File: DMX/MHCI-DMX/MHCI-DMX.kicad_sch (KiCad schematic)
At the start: 39 parts, among them J1 XLR_Male, J2 XLR5_Female, J3 2012670005, J4 Barrel_Jack, K2 G5V-2, U2 TJA1051T, U4 74LVC1G08

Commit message: DMX Schematic complete, and initial Layout
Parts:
- removed C7: 10uF, Capacitor_SMD:C_0603_1608Metric, symbol Device:C_Small
- removed C8: 1uF, Capacitor_SMD:C_0402_1005Metric, symbol Device:C_Small
- removed C9: 100nF, Capacitor_SMD:C_0402_1005Metric, symbol Device:C_Small
- removed D1: D_TVS_Dual_AAC, Package_TO_SOT_SMD:SOT-23, symbol Device:D_TVS_Dual_AAC
- removed FB2: FerriteBead, Diode_SMD:D_0805_2012Metric, symbol Device:FerriteBead_Small
- removed J4: Barrel_Jack, Connector_BarrelJack:BarrelJack_SwitchcraftConxall_RAPC10U_Horizontal, symbol Connector:Barrel_Jack
- removed TP3: VIN, TestPoint:TestPoint_Pad_D1.0mm, symbol Connector:TestPoint
- removed TP4: 5V, TestPoint:TestPoint_Pad_D1.0mm, symbol Connector:TestPoint
- removed U1: ~, MHCI:ESP-32-S3-Zero - SMD, symbol MHCI:ESP32-S3-Zero
- added D1: 1N4148W, Diode_SMD:D_SOD-123, symbol Device:D
- added D2, D4, D6: D_TVS_Dual_AAC, Package_TO_SOT_SMD:SOT-23, symbol Device:D_TVS_Dual_AAC
- added J10, J11, J12, J13, J14, J15: Conn_01x02, MHCI:2060-452-998-404 Wago, symbol Connector_Generic:Conn_01x02
- added J17: Conn_01x08, Connector_PinSocket_2.54mm:PinSocket_1x08_P2.54mm_Vertical, symbol Connector_Generic:Conn_01x08
- added J4, J7, J8: Conn_01x04, Connector_PinSocket_2.54mm:PinSocket_1x04_P2.54mm_Vertical, symbol Connector_Generic:Conn_01x04
- added J5: Conn_01x02, TerminalBlock_Phoenix:TerminalBlock_Phoenix_MPT-0,5-2-2.54_1x02_P2.54mm_Horizontal, symbol Connector_Generic:Conn_01x02
- added J6: Barrel_Jack_MountingPin, Connector_BarrelJack:BarrelJack_GCT_DCJ200-10-A_Horizontal, symbol Connector:Barrel_Jack_MountingPin
- added J9: Conn_01x02, Connector_PinHeader_2.54mm:PinHeader_1x02_P2.54mm_Vertical, symbol Connector_Generic:Conn_01x02
- added JP10, JP11, JP12, JP9: SolderJumper_3_Open, Jumper:SolderJumper-3_P1.3mm_Open_RoundedPad1.0x1.5mm, symbol Jumper:SolderJumper_3_Open
- added JP7, JP8: Jumper_2_Open, Jumper:SolderJumper-2_P1.3mm_Open_RoundedPad1.0x1.5mm, symbol Jumper:Jumper_2_Open
- added Q1: PMOS, Package_TO_SOT_SMD:SOT-23, symbol Simulation_SPICE:PMOS
- added R8: 100k, Resistor_SMD:R_0603_1608Metric, symbol Device:R_US
- added R9: 120R, Resistor_SMD:R_0402_1005Metric, symbol Device:R_US
- added U1, U6, U9: SRV05-4, Package_TO_SOT_SMD:SOT-23-6, symbol Power_Protection:SRV05-4
- added U5: TME-0505S, Converter_DCDC:Converter_DCDC_TRACO_TME_03xxS_05xxS_12xxS_Single_THT, symbol Converter_DCDC:TME-0305S
- added U7: ~, MHCI:ESP-32-S3-Tiny - PTH, symbol MHCI:ESP32-S3-Tiny
- added U8: TXB0108PW, Package_SO:TSSOP-20_4.4x6.5mm_P0.65mm, symbol Logic_LevelTranslator:TXB0108PW
- J1: footprint Connector_Audio:Jack_XLR_Neutrik_NC5FAH-DA_Horizontal -> MHCI:Jack_XLR_Neutrik_NC5MAH_LR
- J2: footprint Connector_Audio:Jack_XLR_Neutrik_NC5FAH-0_Horizontal -> MHCI:Jack_XLR_Neutrik_NC5FAH_LR-DAE
- J3: footprint Landing-Light:MOLEX_2012670005 -> LandingLight:MOLEX_2012670005
- PS1: footprint MCHI:CONV_TBA1-0510 -> MHCI:CONV_TBA1-0510
- U3: footprint (none) -> MHCI:ISO-DMX
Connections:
- net +3V3: now also U7.3V3
- net +5V: now also K2.16, D1.1 (K), J17.1 (Pin_1), J4.1 (Pin_1), J7.1 (Pin_1), J8.1 (Pin_1), U1.5 (VP), U5.2 (+Vin), U6.5 (VP), U9.5 (VP)
- net A: now also R9.1
- net A_OUT: now also D4.1 (A1)
- net B: now also JP8.2 (B)
- net B_OUT: now also D4.2 (A2)
- net CANH: now also JP11.3 (B), JP9.3 (B), U6.6 (IO4)
- net CANL: now also JP10.1 (A), JP12.1 (A), U6.4 (IO3)
- net CAN_RX: now also U7.2 (GPIO2)
- net CAN_S: now also U7.5 (GPIO5)
- net CAN_TX: now also U7.1 (GPIO1)
- net CC1: now also D2.2 (A2)
- net CC2: now also D2.1 (A1)
- net D: now also U7.14 (GPIO14)
- net DE: now also U7.15 (GPIO15)
- net ESP_32_GPIO_12: now also U7.12 (GPIO12)
- net ESP_32_GPIO_13: now also U7.13 (GPIO13)
- net Earth: now also D2.3 (common), J5.2 (Pin_2), J6.2, J9.2 (Pin_2)
- net GND: now also U3.2 (GND), D6.3 (common), J10.2 (Pin_2), J11.2 (Pin_2), J12.2 (Pin_2), J13.2 (Pin_2), J14.2 (Pin_2), J15.2 (Pin_2), J17.8 (Pin_8), J4.4 (Pin_4), J7.4 (Pin_4), J8.4 (Pin_4), JP7.2 (B), Q1.2 (S), R8.2, U1.2 (VN), U5.1 (-Vin), U6.2 (VN), U7.GND, U9.2 (VN)
- net GND_DMX: now also D4.3 (common), U5.3 (-Vout)
- net NRE: now also U7.16 (GPIO16)
- net R: now also U7.17 (GPIO17)
- net SCL: now also U7.3 (GPIO3), U8.1 (A1)
- net SDA: now also U7.4 (GPIO4), U8.3 (A2)
- net VIN: now also J5.1 (Pin_1), J6.1, J9.1 (Pin_1)
- net DMX_EN: now reaches U4.2
- net DMX_EN: now also U7.18 (GPIO18)
- net at U4.4: now also Q1.1 (G), R8.1; no longer K2.16
- net at JP1.1 (A): now also U7.5V
- net +5V_ISO: now reaches U3.7 (5V_ISO)
- net +5V_ISO: now also U5.4 (+Vout)
- net DMX_PASSTHROUGH: now reaches K2.1
- net DMX_PASSTHROUGH: now also D1.2 (A), JP7.1 (A), Q1.3 (D)
- new net: J7.3 (Pin_3), JP12.2 (C)
- new net: J7.2 (Pin_2), JP11.2 (C)
- new net: JP8.1 (A), R9.2
- new net: J4.2 (Pin_2), JP9.2 (C)
- new net: J4.3 (Pin_3), JP10.2 (C)
- new net GPIO_X1: U7.6 (GPIO6), U8.4 (A3)
- new net GPIO_X1_5: J10.1 (Pin_1), J17.2 (Pin_2), U1.1 (IO1), U8.17 (B3)
- new net GPIO_X2: U7.7 (GPIO7), U8.5 (A4)
- new net GPIO_X2_5: J11.1 (Pin_1), J17.3 (Pin_3), U1.3 (IO2), U8.16 (B4)
- new net GPIO_X3: U7.8 (GPIO8), U8.6 (A5)
- new net GPIO_X3_5: J12.1 (Pin_1), J17.4 (Pin_4), U1.4 (IO3), U8.15 (B5)
- new net GPIO_X4: U7.9 (GPIO9), U8.7 (A6)
- new net GPIO_X4_5: J13.1 (Pin_1), J17.5 (Pin_5), U1.6 (IO4), U8.14 (B6)
- new net GPIO_X5: U7.11 (GPIO11), U8.8 (A7)
- new net GPIO_X5_5: J14.1 (Pin_1), J17.6 (Pin_6), U8.13 (B7), U9.1 (IO1)
- new net GPIO_X6: U7.10 (GPIO10), U8.9 (A8)
- new net GPIO_X6_5: J15.1 (Pin_1), J17.7 (Pin_7), U8.12 (B8), U9.3 (IO2)
- new net SCL_5: JP11.1 (A), JP9.1 (A), U6.1 (IO1), U8.20 (B1)
- new net SDA_5: JP10.3 (B), JP12.3 (B), U6.3 (IO2), U8.18 (B2)
- new net UART_RX: J8.3 (Pin_3), U7.RX, U9.4 (IO3)
- new net UART_TX: J8.2 (Pin_2), U7.TX, U9.6 (IO4)
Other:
- note added: "Connectors"
- note added: "Expose full GPIO"
- note added: "Mosfet and driver pins for LED tape"
- note added: "Some 1 Pin Data ports"
- note removed: "Connector"
- note removed: "OR Gate"
- note removed: "Termination Resistor"
- moved on the sheet: C1, C2, C3, C4, C5, C6, FB1, J1, J2, J3, JP1, JP2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

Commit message: MHCI DMX - Finalise schematic and initial layout routing
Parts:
- removed JP10, JP11, JP12, JP9: SolderJumper_3_Open, Jumper:SolderJumper-3_P1.3mm_Open_RoundedPad1.0x1.5mm, symbol Jumper:SolderJumper_3_Open
- removed K2: G5V-2, Relay_THT:Relay_DPDT_Omron_G5V-2, symbol Relay:G5V-2
- removed PS1: TBA1-0510, MHCI:CONV_TBA1-0510, symbol MHCI:TBA1-0510
- removed U2: TJA1051T, Package_SO:SOIC-8_3.9x4.9mm_P1.27mm, symbol Interface_CAN_LIN:TJA1051T
- removed U4: 74LVC1G08, Package_TO_SOT_SMD:SOT-23-5_HandSoldering, symbol 74xGxx:74LVC1G08
- removed U6: SRV05-4, Package_TO_SOT_SMD:SOT-23-6, symbol Power_Protection:SRV05-4
- added D3, D5: D_TVS_Dual_AAC, Package_TO_SOT_SMD:SOT-23, symbol Device:D_TVS_Dual_AAC
- added J16, J18: Conn_01x04, Connector_PinSocket_2.54mm:PinSocket_1x04_P2.54mm_Vertical, symbol Connector_Generic:Conn_01x04
- added JP13, JP14, JP15: SolderJumper_3_Open, Jumper:SolderJumper-3_P1.3mm_Open_RoundedPad1.0x1.5mm, symbol Jumper:SolderJumper_3_Open
- added K1: G6K-2, Relay_SMD:Relay_DPDT_Omron_G6K-2F, symbol Relay:G6K-2
- added U10: ~, MHCI:WirelessDMX-Module, symbol MHCI:WirelessDMX-Module
- added U11: TJA1051T-3, Package_SO:SOIC-8_3.9x4.9mm_P1.27mm, symbol Interface_CAN_LIN:TJA1051T-3
- added U4: TEC2-1210WI, Converter_DCDC:Converter_DCDC_TRACO_TMR-xxxx_THT, symbol Converter_DCDC:TEC2-1210WI
- D2, J3, R6, R7: now not fitted; now left out of the parts list
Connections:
- net +3V3: now also U3.1 (5V), U8.10 (OE), U8.2 (V_{CCA}), JP15.1 (A), U10.1 (VCC), U10.11 (VCC), U11.5 (VIO), U4.6 (+VOUT)
- net +5V: now also J16.1 (Pin_1), J18.1 (Pin_1), JP13.3 (B), JP14.3 (B), JP15.3 (B), K1.8, U11.3 (VCC), U4.2 (+VIN); no longer U3.1 (5V)
- net A: now also JP5.1 (A), K1.4; no longer JP5.2 (C)
- net A_IN: now also K1.2
- net A_OUT: now also JP5.2 (C), K1.3; no longer JP5.1 (A)
- net B: now also JP6.1 (A), K1.5; no longer JP6.2 (C)
- net B_IN: now also K1.7
- net B_OUT: now also JP6.2 (C), K1.6; no longer JP6.1 (A)
- net CANH: now also D5.1 (A1), J16.2 (Pin_2), J18.2 (Pin_2)
- net CANH_L: now also U11.6 (CANL)
- net CANH_T: now also U11.7 (CANH)
- net CANL: now also D5.2 (A2), J16.3 (Pin_3), J18.3 (Pin_3)
- net CAN_RX: now also U11.4 (RXD)
- net CAN_S: now also U11.8 (S)
- net CAN_TX: now also U11.1 (TXD)
- net D: now also U10.3 (DMX_TX)
- net DE: now also U10.4 (DMX_DE)
- net DMX_EN: now also JP13.1 (A)
- net DMX_PASSTHROUGH: now also K1.1
- net Earth: now also JP14.1 (A), U4.1 (-VIN)
- net GND: now also U8.11 (GND), D3.3 (common), D5.3 (common), J16.4 (Pin_4), J18.4 (Pin_4), U10.10 (GND), U10.12 (GND), U10.2 (GND), U11.2 (GND), U4.7 (-VOUT)
- net GPIO_X1: now also U7.11 (GPIO11), U10.9 (SPI_SCK); no longer U7.6 (GPIO6)
- net GPIO_X1_5: now also U1.3 (IO2); no longer U1.1 (IO1)
- net GPIO_X2: now also U7.10 (GPIO10), U10.8 (SPI_MOSI); no longer U7.7 (GPIO7)
- net GPIO_X2_5: now also U1.1 (IO1); no longer U1.3 (IO2)
- net GPIO_X3: now also U7.9 (GPIO9), U10.7 (SPI_MISO); no longer U7.8 (GPIO8)
- net GPIO_X4_5: now also U9.3 (IO2); no longer U1.6 (IO4)
- net GPIO_X5: now also U7.7 (GPIO7), U10.14 (SPI_nSS); no longer U7.11 (GPIO11)
- net GPIO_X5_5: now also U9.6 (IO4); no longer U9.1 (IO1)
- net GPIO_X6: now also U7.6 (GPIO6); no longer U7.10 (GPIO10)
- net GPIO_X6_5: now also U9.4 (IO3); no longer U9.3 (IO2)
- net NRE: now also U10.5 (DMX_RE)
- net R: now also U10.6 (DMX_RX)
- net SCL: now also U10.18 (I2C_SCL)
- net SCL_5: now also J4.2 (Pin_2), J7.2 (Pin_2), D3.2 (A2)
- net SDA: now also U10.17 (I2C_SDA)
- net SDA_5: now also J4.3 (Pin_3), J7.3 (Pin_3), D3.1 (A1)
- net UART_RX: now also D6.1 (A1); no longer U9.4 (IO3)
- net UART_TX: now also D6.2 (A2); no longer U9.6 (IO4)
- net at U8.19 (V_{CCB}): now also JP15.2 (C)
- net at Q1.1 (G), R8.1: now also JP13.2 (C)
- net ESP_32_GPIO_12 renamed I2C_nATTN
- net I2C_nATTN: now also U10.16 (I2C_nATTN)
- net ESP_32_GPIO_13 renamed SPI_nATTN
- net SPI_nATTN: now also U10.13 (SPI_nATTN)
- net GPIO_X4 renamed CTI_RESET
- net CTI_RESET: now also U7.8 (GPIO8), U10.15 (CTI_RESET); no longer U7.9 (GPIO9)
- new net: JP14.2 (C), U4.3 (ON/~{OFF})
- no-connect marks 19 -> 21
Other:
- note added: "Check the voltages here"
- note added: "RS3K-053.3S/H3"
- note removed: "Expose full GPIO"
- note removed: "Mosfet and driver pins for LED tape"
- note removed: "Some 1 Pin Data ports"
- moved on the sheet: C1, C2, C3, C4, C5, C6, D1, D4, D6, FB1, J1, J10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

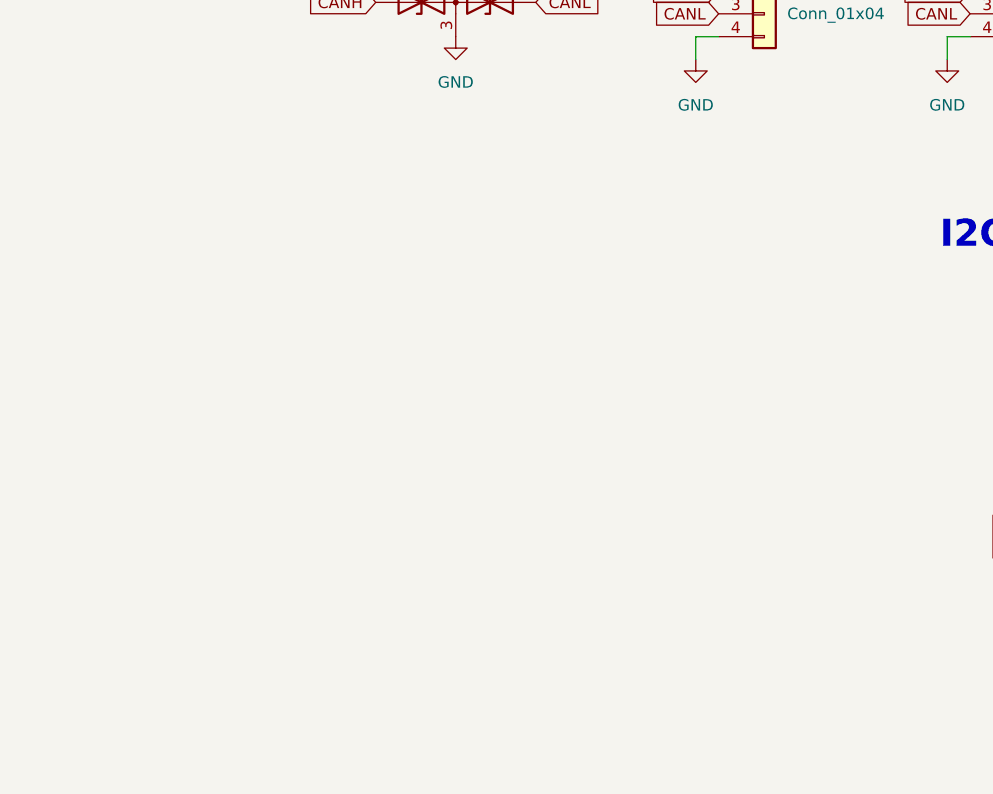
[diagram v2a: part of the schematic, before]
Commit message: Adding LEDs to DMX plug and socket.
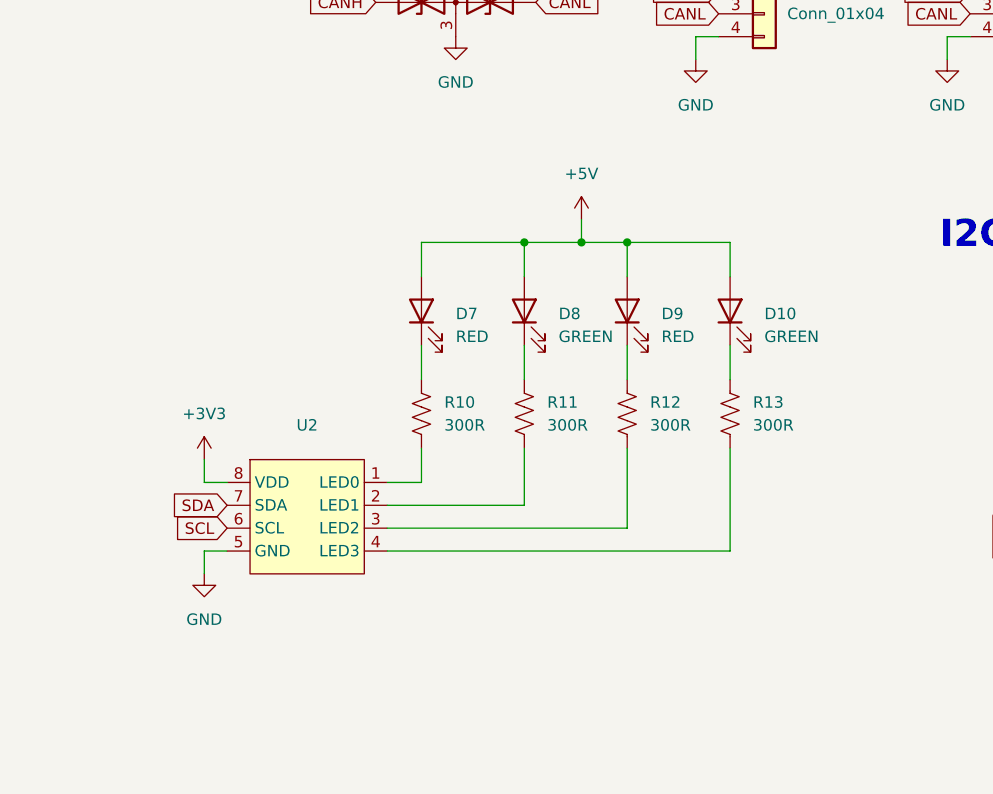
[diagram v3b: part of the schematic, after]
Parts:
- added D10, D8: GREEN, LED_SMD:LED_0603_1608Metric, symbol Device:LED
- added D7, D9: RED, LED_SMD:LED_0603_1608Metric, symbol Device:LED
- added R10, R11, R12, R13: 300R, Resistor_SMD:R_0603_1608Metric, symbol Device:R_US
- added U2: ~, Package_SO:TSSOP-8_3x3mm_P0.65mm, symbol MHCI:PCA9633
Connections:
- net +3V3: now also U2.8 (VDD)
- net +5V: now also D10.2 (A), D7.2 (A), D8.2 (A), D9.2 (A)
- net GND: now also U2.5 (GND)
- net SCL: now also U2.6 (SCL)
- net SDA: now also U2.7 (SDA)
- new net: D7.1 (K), R10.1
- new net: D8.1 (K), R11.1
- new net: D9.1 (K), R12.1
- new net: R12.2, U2.3 (LED2)
- new net: R10.2, U2.1 (LED0)
- new net: R11.2, U2.2 (LED1)
- new net: R13.2, U2.4 (LED3)
- new net: D10.1 (K), R13.1

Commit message: Logos and description
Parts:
- added H1, H2, H3, H4: MountingHole, MountingHole:MountingHole_3.2mm_M3, symbol Mechanical:MountingHole
- U2: LCSC (none) -> C88381

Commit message: Update DMX board with v1.1 updates
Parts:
- added D11, D12, D13: RED, LED_SMD:LED_0603_1608Metric, symbol Device:LED
- added R14, R15, R16: 680R, Resistor_SMD:R_0603_1608Metric, symbol Device:R_US
- added R17, R18, R19, R20, R21, R22: 1K, Resistor_SMD:R_0603_1608Metric, symbol Device:R_US
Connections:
- net +3V3: now also D13.2 (A)
- net +5V: now also D11.2 (A)
- net +5V_ISO: now also D12.2 (A)
- net Earth: now also U5.1 (-Vin), R14.2
- net GND: now also R16.2; no longer U5.1 (-Vin)
- net GND_DMX: now also R15.2
- net GPIO_X1_5: now also R17.2; no longer U8.17 (B3)
- net GPIO_X2_5: now also R18.2; no longer U8.16 (B4)
- net GPIO_X3_5: now also R19.2; no longer U8.15 (B5)
- net GPIO_X4_5: now also R20.2; no longer U8.14 (B6)
- net GPIO_X5_5: now also R21.2; no longer U8.13 (B7)
- net GPIO_X6_5: now also R22.2; no longer U8.12 (B8)
- new net: D13.1 (K), R16.1
- new net: R20.1, U8.14 (B6)
- new net: R22.1, U8.12 (B8)
- new net: R21.1, U8.13 (B7)
- new net: R19.1, U8.15 (B5)
- new net: R18.1, U8.16 (B4)
- new net: R17.1, U8.17 (B3)
- new net: D12.1 (K), R15.1
- new net: D11.1 (K), R14.1
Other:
- moved on the sheet: JP15, U8

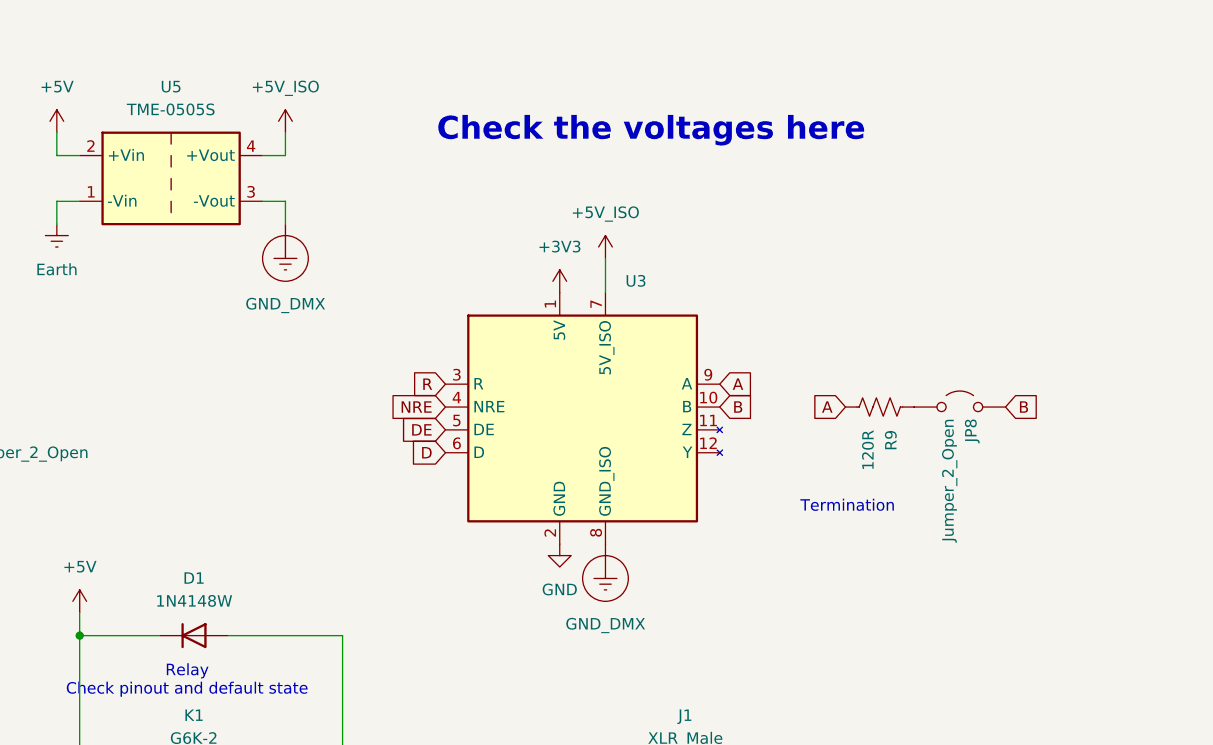
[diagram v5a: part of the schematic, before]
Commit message: MHCI-DMX v1.1 hardware
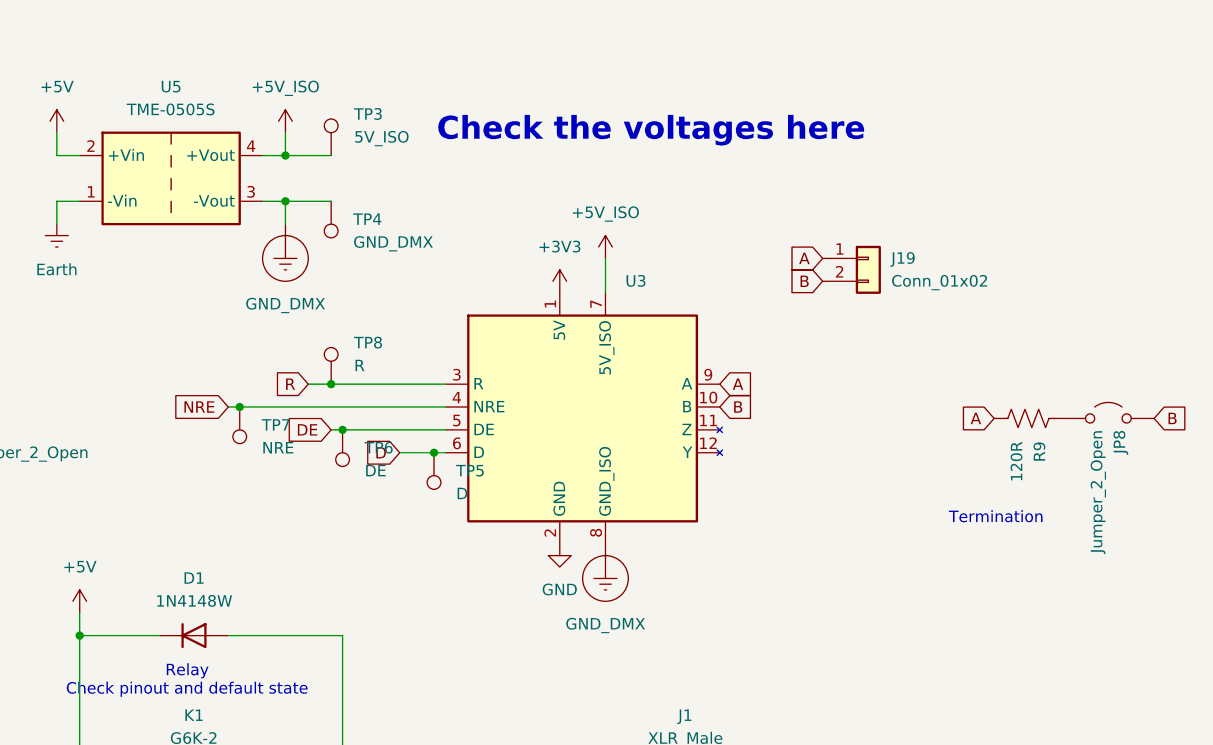
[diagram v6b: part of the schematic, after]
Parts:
- added J19: Conn_01x02, Connector_PinHeader_2.54mm:PinHeader_1x02_P2.54mm_Vertical, symbol Connector_Generic:Conn_01x02
- added TP3: 5V_ISO, TestPoint:TestPoint_Pad_D1.0mm, symbol Connector:TestPoint
- added TP4: GND_DMX, TestPoint:TestPoint_Pad_D1.0mm, symbol Connector:TestPoint
- added TP5: D, TestPoint:TestPoint_Pad_D1.0mm, symbol Connector:TestPoint
- added TP6: DE, TestPoint:TestPoint_Pad_D1.0mm, symbol Connector:TestPoint
- added TP7: NRE, TestPoint:TestPoint_Pad_D1.0mm, symbol Connector:TestPoint
- added TP8: R, TestPoint:TestPoint_Pad_D1.0mm, symbol Connector:TestPoint
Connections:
- net +5V_ISO: now also TP3.1
- net A: now also J19.1 (Pin_1)
- net B: now also J19.2 (Pin_2)
- net D: now also TP5.1
- net DE: now also TP6.1
- net GND_DMX: now also TP4.1
- net NRE: now also TP7.1
- net R: now also TP8.1
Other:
- moved on the sheet: JP8, R9

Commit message: MHCI DMX v1.2 production files
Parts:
- removed D2: D_TVS_Dual_AAC, Package_TO_SOT_SMD:SOT-23, symbol Device:D_TVS_Dual_AAC
- removed J3: 2012670005, LandingLight:MOLEX_2012670005, symbol ESP32_Dev_Board-eagle-import:2012670005
- removed J5: Conn_01x02, TerminalBlock_Phoenix:TerminalBlock_Phoenix_MPT-0,5-2-2.54_1x02_P2.54mm_Horizontal, symbol Connector_Generic:Conn_01x02
- removed J9: Conn_01x02, Connector_PinHeader_2.54mm:PinHeader_1x02_P2.54mm_Vertical, symbol Connector_Generic:Conn_01x02
- removed R6, R7: 5.1k, Resistor_SMD:R_0603_1608Metric, symbol Device:R_US
- removed TP1: VIN, TestPoint:TestPoint_Pad_D1.0mm, symbol Connector:TestPoint
- removed TP2: 5V, TestPoint:TestPoint_Pad_D1.0mm, symbol Connector:TestPoint
- added J3: Conn_01x02, Connector_PinHeader_2.54mm:PinHeader_1x02_P2.54mm_Vertical, symbol Connector_Generic:Conn_01x02
- added J5: Conn_01x04, Connector_PinHeader_2.54mm:PinHeader_1x04_P2.54mm_Vertical, symbol Connector_Generic:Conn_01x04
- added U6: TSR_2-2450, Converter_DCDC:Converter_DCDC_TRACO_TSR-1_THT, symbol Regulator_Switching:TSR_1-2450
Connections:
- net Earth is gone; now on net GND: C4.2, C5.1, C6.2, J6.2, JP14.1 (A), R14.2, U4.1 (-VIN), U5.1 (-Vin)
- net VIN is gone; now on net +5V: C4.1, C5.2, FB1.1, J6.1
- net +3V3: now also J3.1 (Pin_1)
- net +5V: now also J5.4 (Pin_4), U6.3 (Vout); no longer C6.1, FB1.2, JP14.3 (B), U4.2 (+VIN)
- net GND: now also J3.2 (Pin_2), J5.2 (Pin_2), J5.3 (Pin_3), U6.2 (GND)
- new net 5V filtered: C6.1, FB1.2, JP14.3 (B), U4.2 (+VIN)
- new net VCC: J5.1 (Pin_1), U6.1 (Vin)
- no-connect marks 21 -> 7
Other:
- note added: "5V 2A"
- note added: "5V in"
- note added: "6.5-36Vin"
- note removed: "10%"
- note removed: "Check the voltages here"
- note removed: "Power In"
- note removed: "USB-C Connector"
- moved on the sheet: D11, D12, D13, R14, R15, R16
